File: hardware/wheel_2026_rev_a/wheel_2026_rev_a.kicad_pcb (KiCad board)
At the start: 2 copper layers, 48 x 20 mm, 19 parts, among them J1 OTHER, J2 RPI, U1 LM358, U2 TCRT5000, U3 MLX90614

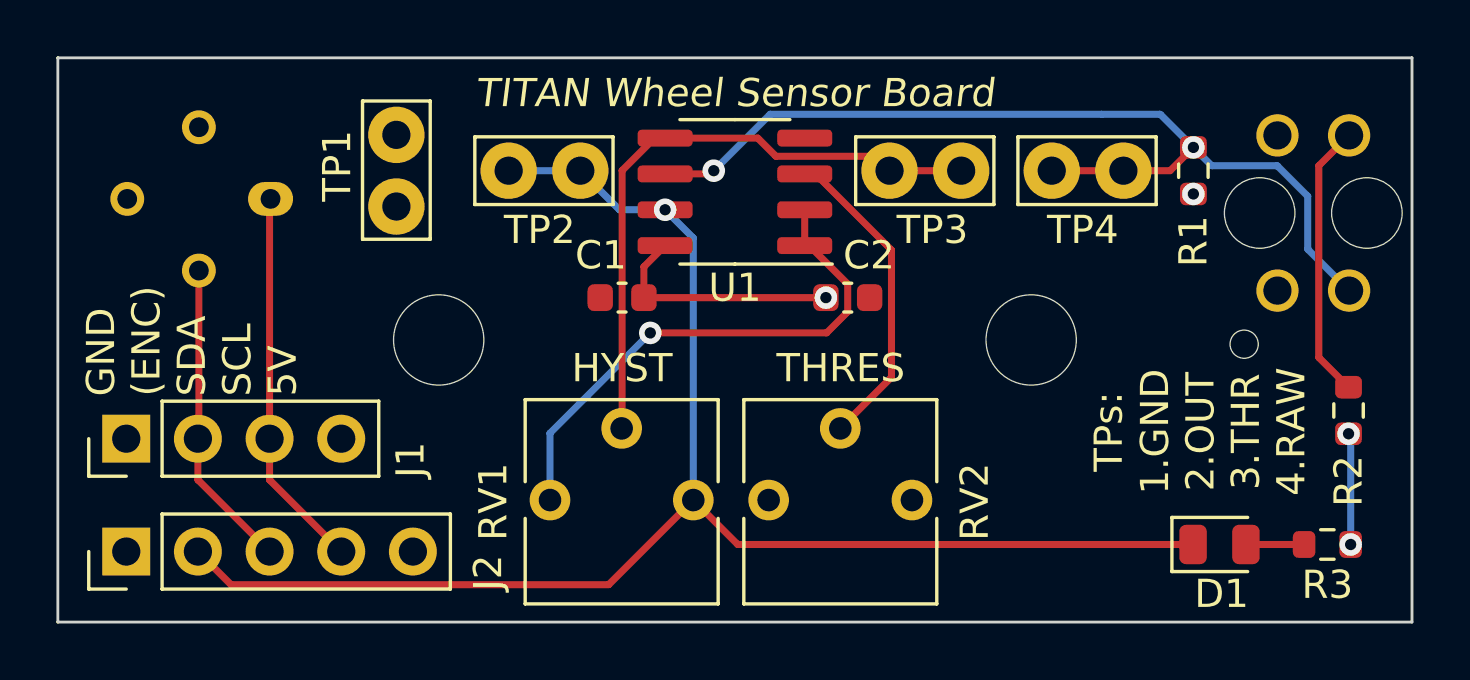
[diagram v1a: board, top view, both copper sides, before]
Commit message: Revised wheel sensor board and documentation
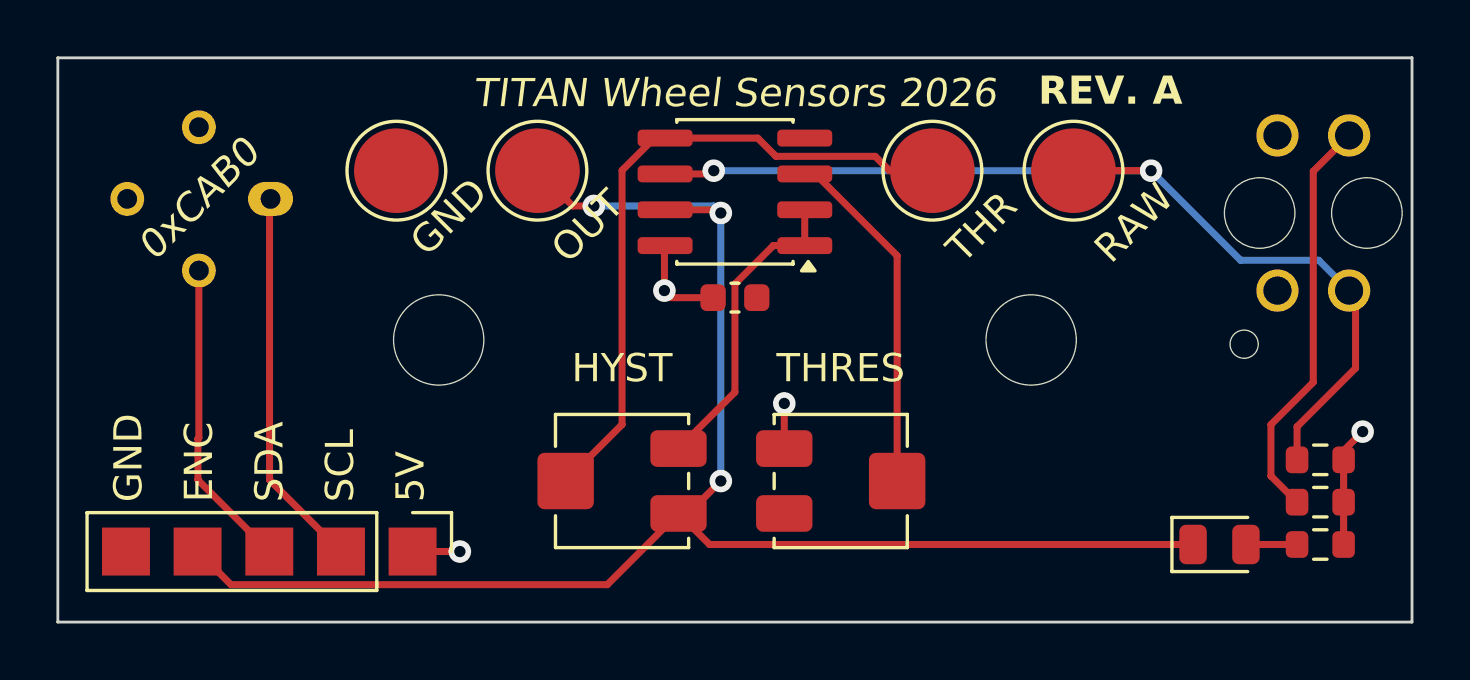
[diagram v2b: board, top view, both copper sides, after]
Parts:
- removed C1: 0u1, Capacitor_SMD:C_0603_1608Metric
- removed J1: OTHER, Connector_PinHeader_2.54mm:PinHeader_1x04_P2.54mm_Vertical
- removed U2: TCRT5000, TCRT5000:OPTO_TCRT5000
- added U4: TLV2372IDR, Package_SO:SOIC-8_3.9x4.9mm_P1.27mm, F.Cu at (144.0, 43.8)
- J2: footprint Connector_PinHeader_2.54mm:PinHeader_1x05_P2.54mm_Vertical -> TITAN:WirePads_1x05_P2.54mm
- R3: value 1k -> 330
- RV1, RV2: footprint Potentiometer_THT:Potentiometer_Vishay_T73YP_Vertical -> Potentiometer_SMD:Potentiometer_Bourns_3314J_Vertical
- TP1, TP2, TP3, TP4: footprint TestPoint:TestPoint_Bridge_Pitch2.54mm_Drill1.0mm -> TestPoint:TestPoint_Pad_D3.0mm
- U1: value LM358 -> TCRT5000; footprint Package_SO:SOIC-8_3.9x4.9mm_P1.27mm -> TITAN:OPTO_TCRT5000; moved to B.Cu
- U3: value MLX90614 -> MLX90614xSF-AxA-000-TU
- moved U1 20.5 mm to (164.5, 44.5), turned to 90 degrees
- moved R1 11.2 mm to (164.8, 53.2), turned to 180 degrees
- moved J2 10.1 mm to (132.6, 56.5), turned to -90 degrees
- moved C2 4.00 mm to (144.0, 47.5)
- moved R2 3.40 mm to (164.8, 54.8), turned to 0 degrees
- moved RV1 2.61 mm to (140.0, 54.0), turned to -90 degrees
- moved RV2 2.61 mm to (147.8, 54.0)
- moved TP3 1.52 mm to (151.0, 43.0)
- moved TP1 1.27 mm to (132.0, 43.0)
- moved TP2 1.02 mm to (137.0, 43.0)
- moved TP4 0.77 mm to (156.0, 43.0)
- moved R3 0.25 mm to (164.8, 56.2), turned to 0 degrees
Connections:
- D1 pad 2: Net-(D1-Pad2) -> Net-(D1-A)
- J2 pad 1: GND -> +5V
- J2 pad 2: /ENCODER_{OUT} -> /SCL
- J2 pad 4: /SCL -> /ENCODER_{OUT}
- J2 pad 5: +5V -> GND
- R2 pad 1: Net-(U2-PadA) -> Net-(R2-Pad1)
- R3 pad 1: +5V -> Net-(D1-A)
- R3 pad 2: Net-(D1-Pad2) -> +5V
- U1 pad 1: /THRES_{BUFFERED} -> Net-(R2-Pad1)
- U1 pad 2: /THRES_{BUFFERED} -> GND
- U1 pad 3: /THRESHOLD -> GND
- U1 pad 4: GND -> /REFLECTIVITY
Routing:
- net Net-(R2-Pad1): track 0.00 -> 14.5 mm
- net Net-(U2-PadA): track 9.81 -> 0.00 mm
- net /THRES_{BUFFERED}: track 19.0 -> 11.0 mm, vias 1 -> 0
- net /ENCODER_{OUT}: track 54.4 -> 57.8 mm, vias 1 -> 3
- net Net-(D1-Pad2): track 2.06 -> 0.00 mm
- net Net-(D1-A): track 0.00 -> 2.06 mm
- net /THRES_{HYSTERESIS}: track 22.1 -> 23.8 mm
- net /REFLECTIVITY: track 34.2 -> 35.8 mm
- net +5V: track 12.6 -> 11.0 mm
- net /THRESHOLD: track 11.3 -> 12.5 mm
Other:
- board text added: "0xCAB0"
- board text added: "5V"
- board text added: "ENC"
- board text added: "GND"
- board text added: "Holes for sensors plotted in layer USER1"
- board text added: "M3s, 21mm apart"
- board text added: "OUT"
- board text added: "RAW"
- board text added: "REV. ${REVISION}"
- board text added: "SCL"
- board text added: "SDA"
- board text added: "THR"
- board text added: "TITAN Wheel Sensors 2026"
- board text added: "h0t hawt HOT!"
- board text removed: "1.GND 2.OUT 3.THR 4.RAW"
- board text removed: "GND (ENC) SDA SCL 5V"
- board text removed: "M3 mounting holes"
- board text removed: "TITAN Wheel Sensor Board"
- board text removed: "TPs:"

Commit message: Wheel rev A PCB as ordered
Added note to use 3.3V power but 5V was endured before without issue.
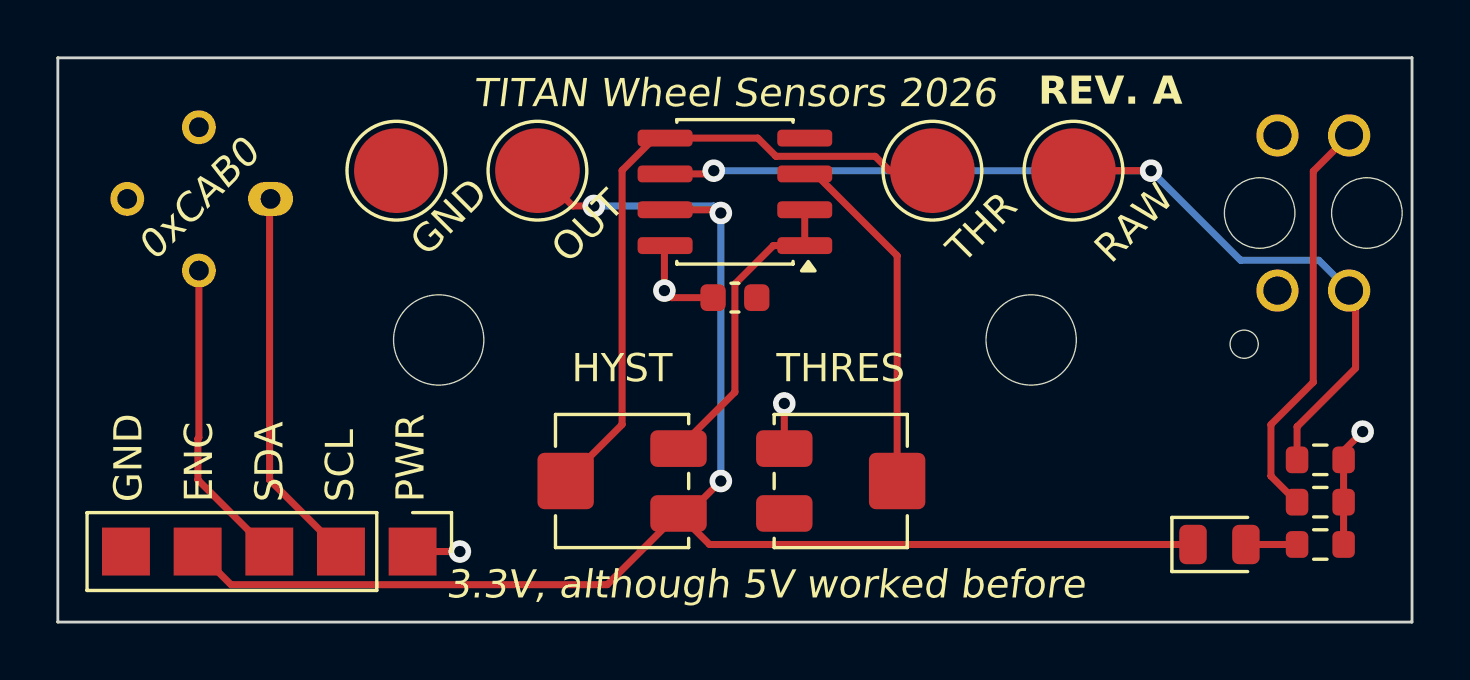
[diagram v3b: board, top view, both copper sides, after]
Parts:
- U3: value MLX90614xSF-AxA-000-TU -> MLX90614ESF-BAA
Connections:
- net +5V renamed VBUS
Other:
- board text added: "3.3V, although 5V worked before"
- board text added: "PWR"
- board text removed: "5V"
